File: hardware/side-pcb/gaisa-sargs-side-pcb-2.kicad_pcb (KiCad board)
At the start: 2 copper layers, 48.1 x 94.9 mm, 1 part

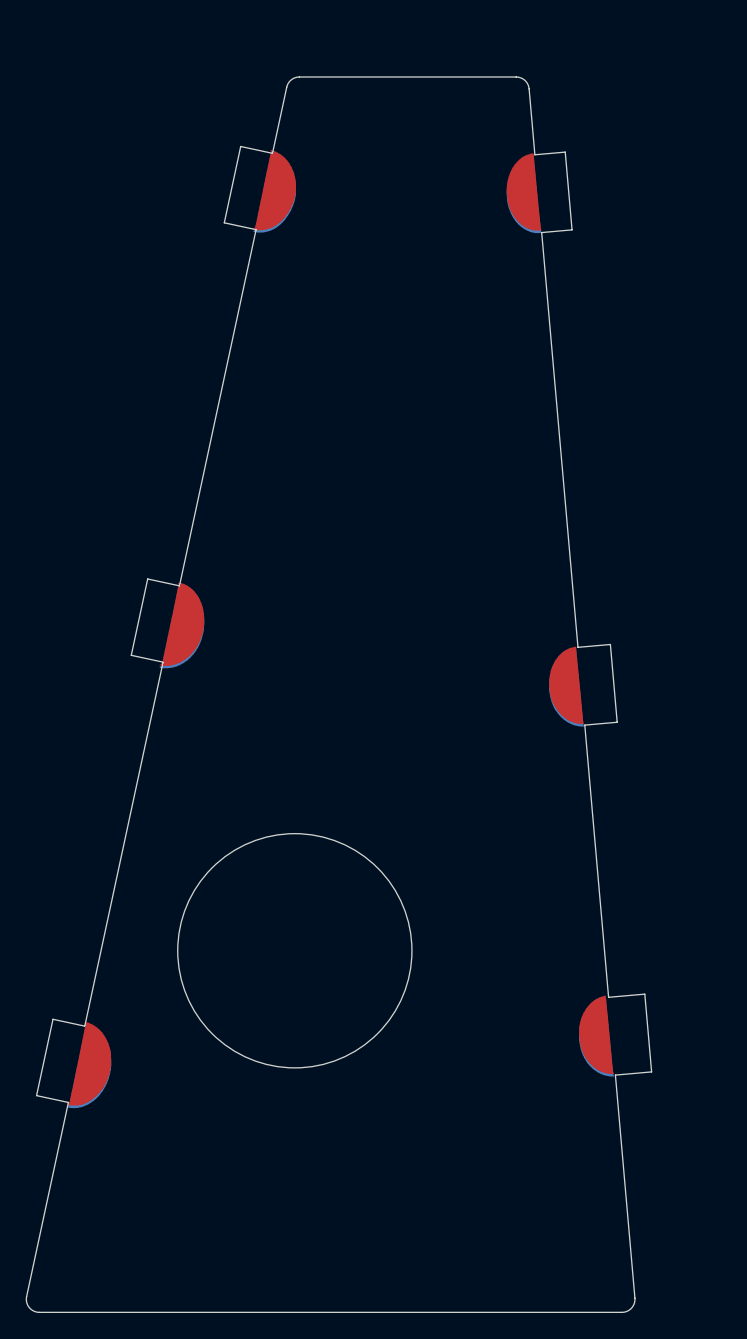
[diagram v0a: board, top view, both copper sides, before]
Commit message: updated side pcb to have cutout for weird devkitc interpretations
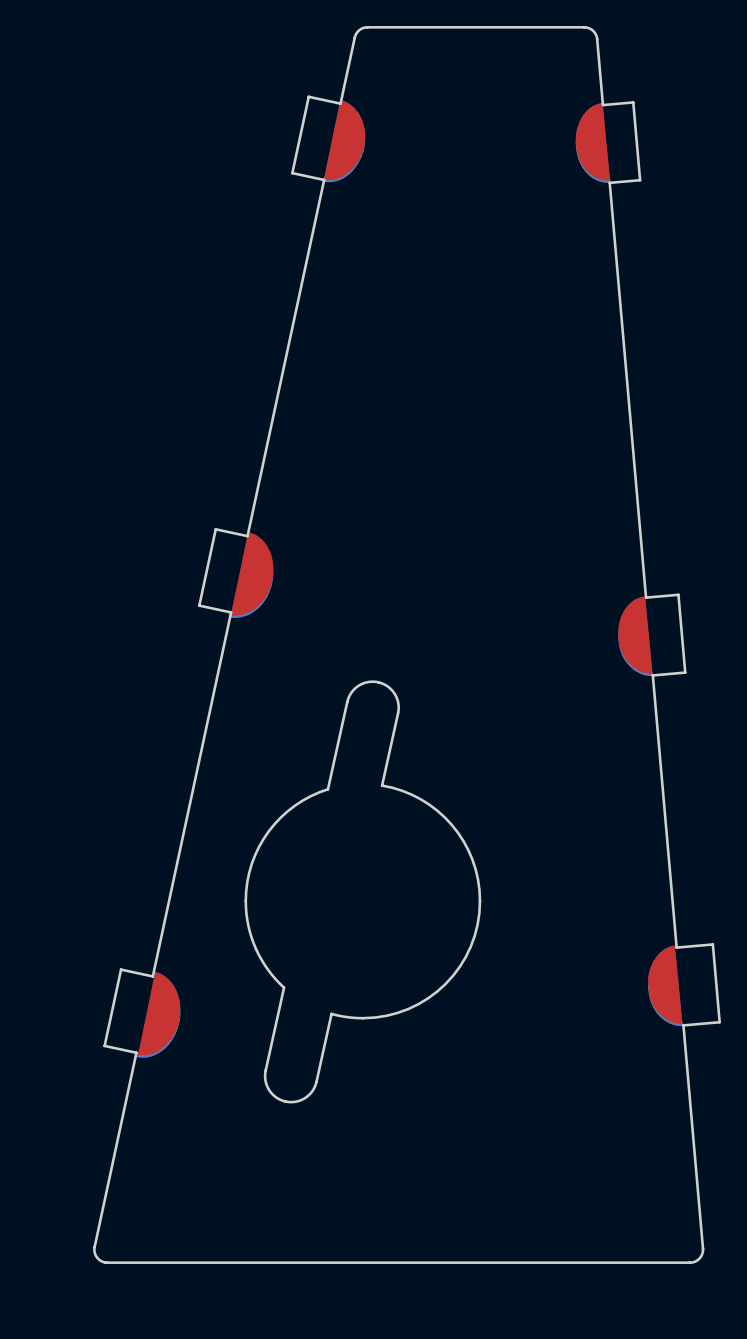
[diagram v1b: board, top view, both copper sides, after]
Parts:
- moved Ref** 6.57 mm to (153.7, 140.2)
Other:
- outline, holes or cut-outs redrawn
